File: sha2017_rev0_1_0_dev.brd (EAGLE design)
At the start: 95 x 86 mm, 193 parts, among them IC1 CP210X_USB_UART, IC2 AP7215, IC3 ESP32WROOM32, IC4 MCP73833, IC5 FXL6408, IC6 CPT112, Q1 MOSFET-PCHANNEL, Q2 MMBT2222A, Q3 MMBT2222A, Q4 MMBT2222A, Q5 MMBT2222A, Q6 SI1304 BDL, Q7 MMBT2222A, Q8 MOSFET-PCHANNEL, T1 SI2301DS, X1 JST-PH3, X2 2908-05WB-MG

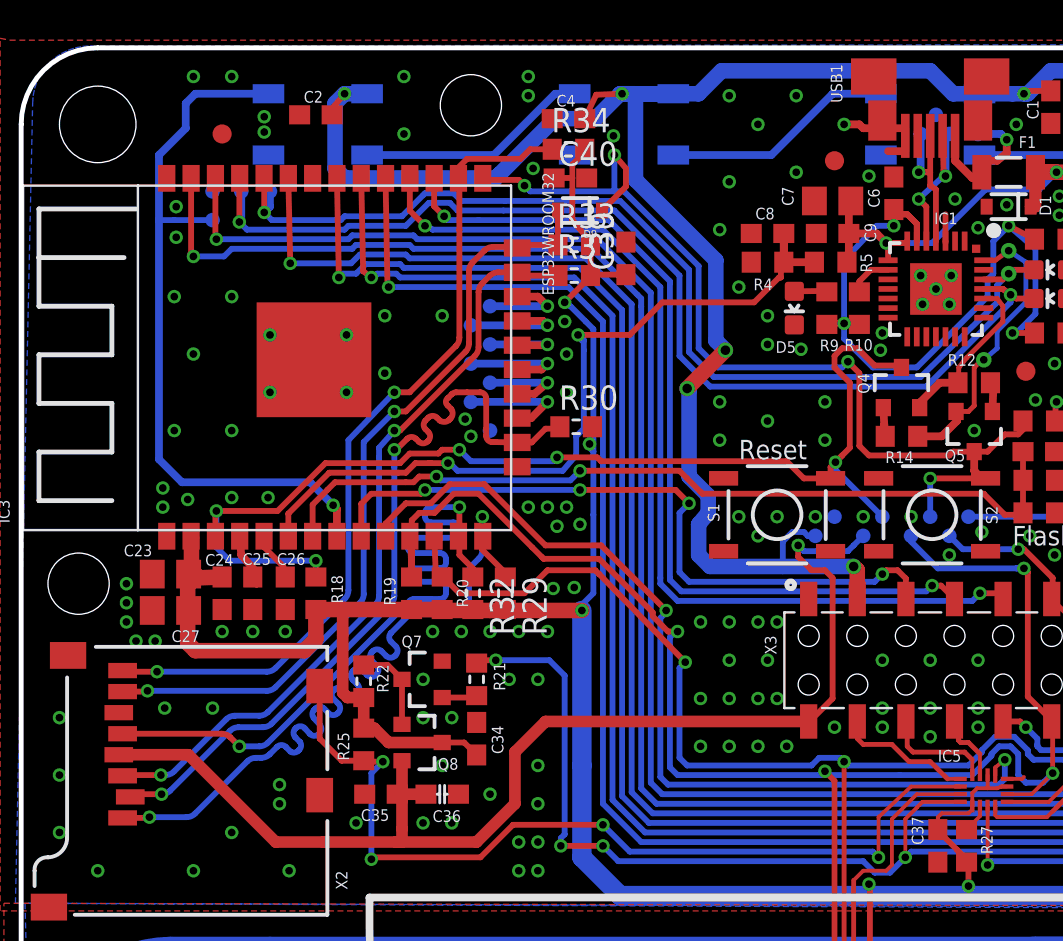
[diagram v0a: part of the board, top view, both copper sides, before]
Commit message: add solder briges to unused IOs at 1 Wire SDiomode (roosted: MIMIMI I WANT MORE IOS!!!!!)
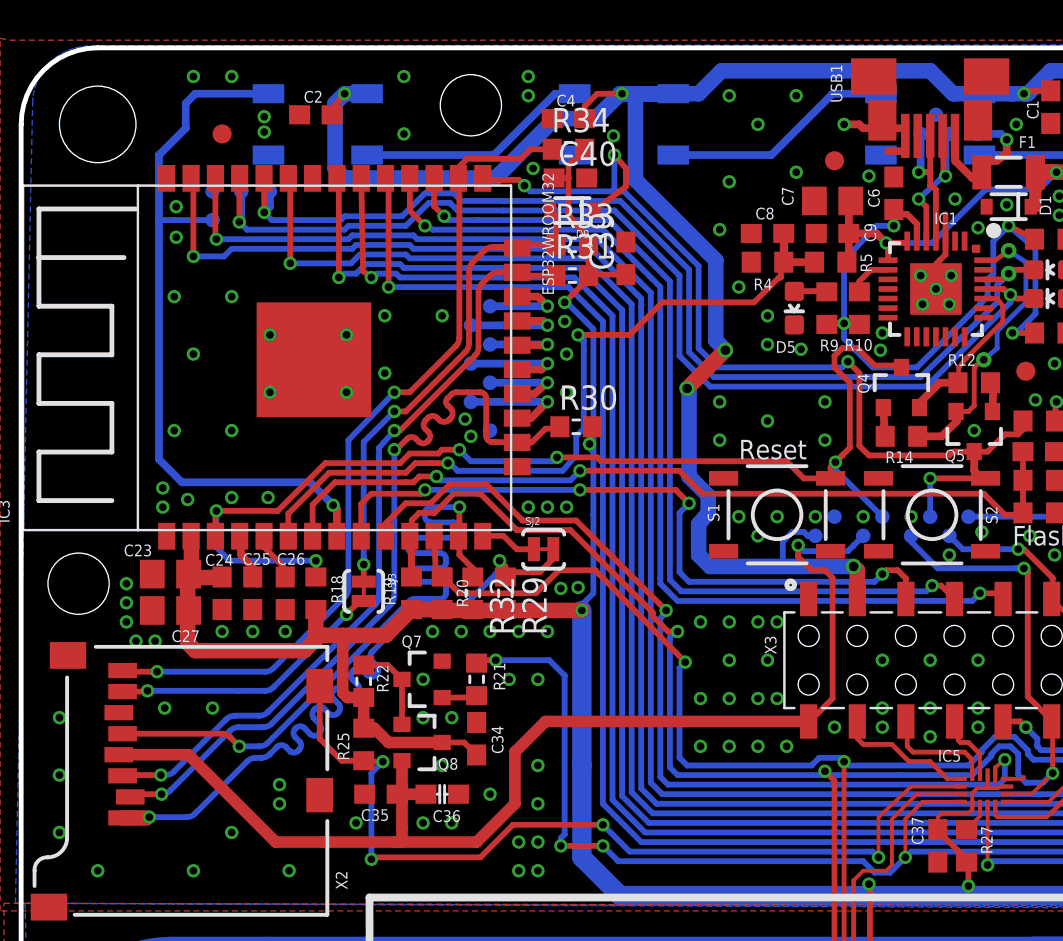
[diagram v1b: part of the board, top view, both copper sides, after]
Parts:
- added SJ2, SJ3: JUMPER-PAD-2-NC_BY_TRACE, SparkFun-Passives:PAD-JUMPER-2-NC_BY_TRACE_YES_SILK
- moved D9 0.40 mm to (28.8, 76.5)
- moved R31 0.10 mm to (28.8, 73.1)
- moved R33 0.10 mm to (28.8, 74.7)
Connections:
- new net N$20: SJ3.2, X2.7
- new net SD_DATA2_OUT: R29.1, SJ2.2, X2.1
- net SD_DATA0: now also SJ3.1; no longer X2.7
- net SD_DATA2: now also SJ2.1; no longer R29.1, X2.1
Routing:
- net SD_DATA2_OUT: track 0.00 -> 36.1 mm, vias 0 -> 2
- net SD_DATA2: track 38.5 -> 2.97 mm, vias 2 -> 0
- net SD_DATA0: track 41.4 -> 26.4 mm
- net N$20: track 0.00 -> 14.5 mm, vias 0 -> 2
- net GND: track 13.8 -> 15.0 mm, vias 276 -> 274
- net +3V3: track 270.4 -> 269.8 mm

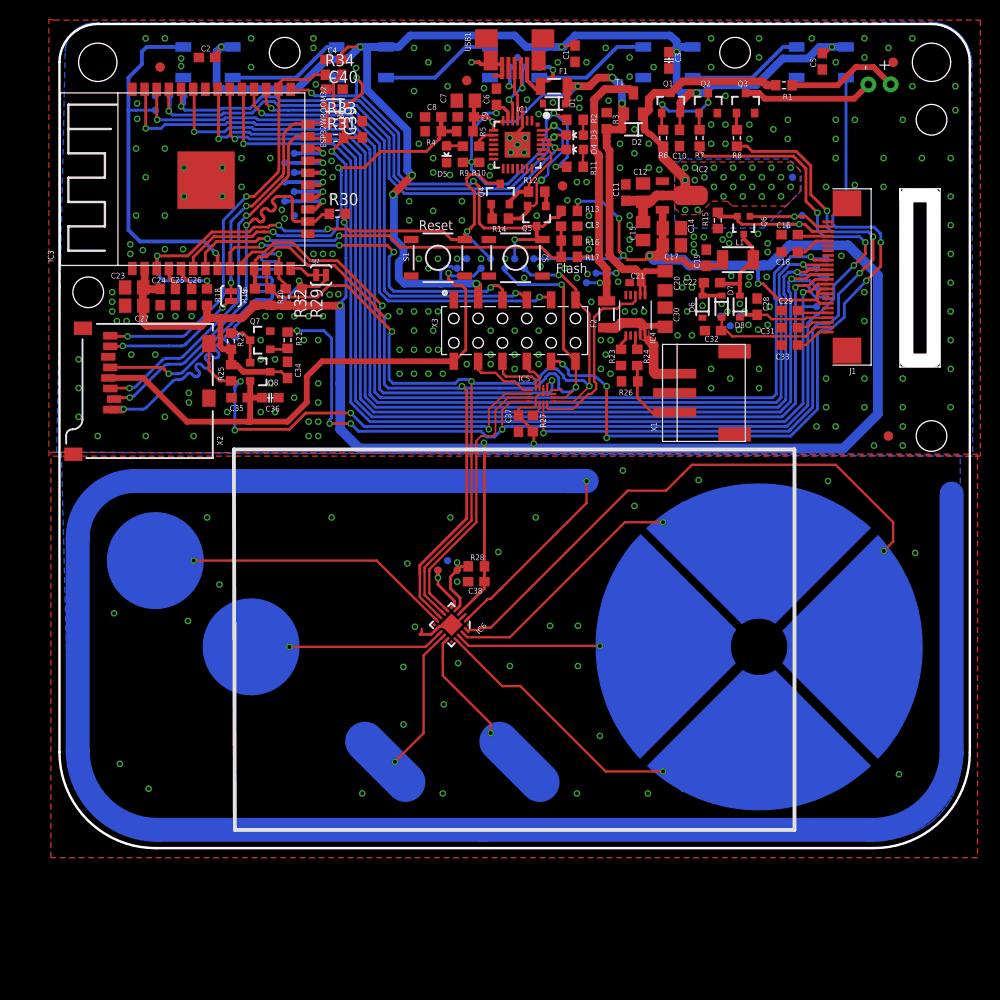
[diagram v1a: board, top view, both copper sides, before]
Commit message: fixed designators
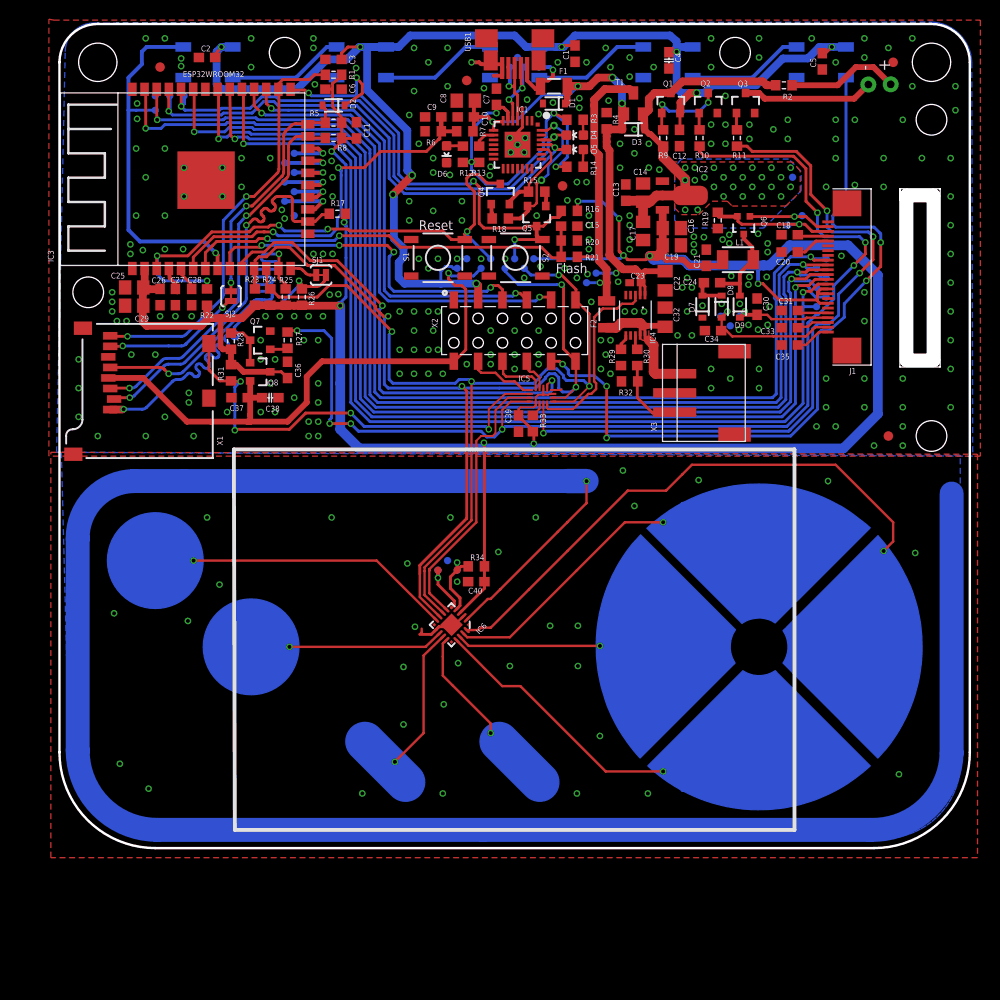
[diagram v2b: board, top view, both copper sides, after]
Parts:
- removed SJ3: JUMPER-PAD-2-NC_BY_TRACE, SparkFun-Passives:PAD-JUMPER-2-NC_BY_TRACE_YES_SILK
- removed U$26, U$27, U$28: VIA, badge:VIA
- added $$U$1, $$U$2, $$U$3: VIA, badge:VIA
- added SJ1: JUMPER-PAD-2-NC_BY_TRACE, SparkFun-Passives:PAD-JUMPER-2-NC_BY_TRACE_YES_SILK
- C12, C15, C7: value 4u7/16V -> 100n; device rcl:C0805 -> rcl:C0603
- C16, C29: value 1u -> 4u7/16V; device rcl:C0603 -> rcl:C0805
- C19, C8: value 100n -> 4u7/16V; device rcl:C0603 -> rcl:C0805
- C20, C30: value 10uF -> 1u; device rcl:C0805K -> rcl:C0603
- C21: value 100nF -> 100n; device rcl:C0402K -> rcl:C0603
- C22, C32: value 1u -> 10uF; device rcl:C0603 -> rcl:C0805K
- C23: value 4u7/16V -> 100nF; device rcl:C0805 -> rcl:C0402K
- C24, C35: value 100n -> 1u
- C25: value (none) -> 4u7/16V; device rcl:C0603 -> rcl:C0805
- C26, C37: value (none) -> 100n
- C27: value 4u7/16V -> (none); device rcl:C0805 -> rcl:C0603
- C28: value 1u -> (none)
- C3: value 4u7/16V -> 100n; device 00ralf:C0603-DASHES -> rcl:C0603
- C36: value 4u7/16V -> 1u; device 00ralf:C0603-DASHES -> rcl:C0603
- C38, C4: value 100n -> 4u7/16V; device rcl:C0603 -> 00ralf:C0603-DASHES
- C39: value 100n -> (none)
- D3: value Yellow -> NSVR0320MW2T1G; device SparkFun-LED:LED-0603 -> SparkFun-DiscreteSemi:SOD-323
- D4: value RED -> Yellow
- D5: value green -> RED
- D6: value NSVR0320MW2T1G -> green; device SparkFun-DiscreteSemi:SOD-323 -> SparkFun-LED:LED-0603
- R1: value 10R -> 10k
- R10, R27: device rcl:R0603 -> 00ralf:R0603-DASHES
- R11, R28, R9: value 1k -> 10k; device rcl:R0603 -> 00ralf:R0603-DASHES
- R12, R14, R3: value 10k -> 1k
- R15: value 5R -> 10k; device 00ralf:R0603-DASHES -> rcl:R0603
- R16, R4: value 100k -> 10k
- R17, R5: value 220k -> 10k; device rcl:R0603 -> 00ralf:R0603-DASHES
- R19: value 470R -> 5R; device rcl:R0603 -> 00ralf:R0603-DASHES
- R2: value 1k -> 10R; device rcl:R0603 -> 00ralf:R0603-DASHES
- R20: value 470R -> 100k
- R21, R7: value 10k -> 220k; device 00ralf:R0603-DASHES -> rcl:R0603
- R22, R33: device 00ralf:R0603-DASHES -> rcl:R0603
- R23: value 2.2k -> 470R
- R24: value 1k -> 470R
- R25: value 100k -> 10k; device rcl:R0603 -> 00ralf:R0603-DASHES
- R26: value 150k -> 10k; device rcl:R0603 -> 00ralf:R0603-DASHES
- R29: value 10k -> 2.2k; device 00ralf:R0603-DASHES -> rcl:R0603
- R30, R34: value 10k -> 1k; device 00ralf:R0603-DASHES -> rcl:R0603
- R31, R6: value 10k -> 100k; device 00ralf:R0603-DASHES -> rcl:R0603
- R32: value 10k -> 150k; device 00ralf:R0603-DASHES -> rcl:R0603
- X1: value JST-PH3 -> 2908-05WB-MG; device badge:JST-PH3 -> con-3m:MICRO-SD-SOCKET-PP
- X2: value 2908-05WB-MG -> (none); device con-3m:MICRO-SD-SOCKET-PP -> EAGLE-BOARD-TO-BOARD_CONNECTORS-rev16c:610X12243021
- X3: value (none) -> JST-PH3; device EAGLE-BOARD-TO-BOARD_CONNECTORS-rev16c:610X12243021 -> badge:JST-PH3
- moved $$U$8 83.8 mm to (5.70, 23.5)
- moved C29 68.4 mm to (7.80, 55.6), turned to 180 degrees
- moved C28 59.0 mm to (13.8, 56.5), turned to 90 degrees
- moved C35 57.7 mm to (76.2, 51.5), turned to 0 degrees
- moved C24 57.6 mm to (68.1, 58.0), turned to 0 degrees
- moved C40 53.5 mm to (43.5, 26.8), turned to 180 degrees
- moved R34 53.4 mm to (43.5, 28.4)
- moved C23 52.3 mm to (60.1, 58.0), turned to 0 degrees
- moved U$20 52.0 mm to (87.6, 6.70)
- moved R19 49.0 mm to (68.7, 64.5), turned to 270 degrees
- moved X1 48.7 mm to (16.0, 53.7), turned to 90 degrees
- moved U$11 48.4 mm to (54.1, 22.2)
- moved U$23 47.6 mm to (40.0, 4.70)
- moved U$21 47.4 mm to (9.30, 5.20)
- moved D9 47.1 mm to (71.0, 55.5), turned to 90 degrees
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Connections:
- net +3V3: now also C11.1, C16.1, C21.1, C25.1, C26.1, C29.1, C36.1, C6.1, R1.2, R16.2, R17.2, R22.1, R23.1, R24.1, R25.2, R26.2, R31.1, R33.1, R5.2, R8.2; no longer C14.1, C17.1, C23.1, C24.1, C27.1, C34.1, C37.1, C38.1, R13.2, R18.1, R19.1, R20.1, R22.2, R25.1, R27.1, R29.2, R30.2, R31.2, R32.2, R33.2
- net +5V: now also C10.1, C22.2, C23.2, C8.1, D3.A, R4.2, R7.2; no longer C20.2, C21.2, C7.1, C9.1, D2.A, R3.2, R5.2
- net 3V3_SWITCHED: now also C37.1, C38.1, X1.4, X2.12; no longer C35.1, C36.1, X2.4, X3.12
- net ESP32_!RESET: now also R22.2; no longer R18.2
- net ESP32_FLASH: now also D2.C, R16.1; no longer D9.C, R13.1
- net ESP32_RX: now also D4.C; no longer D3.C
- net ESP32_TX: now also D5.C; no longer D4.C
- net EXTIO-0: now also X2.3; no longer X3.3
- net EXTIO-1: now also X2.4; no longer X3.4
- net EXTIO-2: now also X2.5; no longer X3.5
- net EXTIO-3: now also X2.9; no longer X3.9
- net EXTIO-4: now also X2.10; no longer X3.10
- net EXTIO-5: now also X2.11; no longer X3.11
- net GND: now also $$U$1.P$1, $$U$2.P$1, $$U$3.P$1, C10.2, C12.1, C16.2, C21.2, C22.1, C23.1, C25.2, C26.2, C27.1, C29.2, C3.1, C34.1, C35.1, C4.2, D7.C, R19.2, R20.1, R29.1, R32.1, R6.1, X1.6, X1.CD2, X1.GND1, X1.GND3, X2.1, X3.2; no longer C10.1, C12.2, C16.1, C21.1, C23.2, C24.2, C25.1, C26.1, C27.2, C29.1, C3.2, C34.2, C35.2, C4.1, D5.C, R15.2, R16.1, R23.1, R26.1, R3.1, U$26.P$1, U$27.P$1, U$28.P$1, X1.2, X2.6, X2.CD2, X2.GND1, X2.GND3, X3.1
- net I2C_SCL: now also R24.2, X2.6; no longer R20.2, X3.6
- net I2C_SDA: now also R23.2, X2.7; no longer R19.2, X3.7
- net N$10: now also R15.1; no longer R12.1
- net N$11: now also R18.1; no longer R14.1
- net N$13: now also R15.2; no longer R12.2
- net N$14: now also R18.2; no longer R14.2
- net N$15: now also R27.2; no longer R21.2
- net N$17: now also R28.1; no longer R22.1
- net N$18: now also R2.1; no longer R1.1
- net N$20: now also SJ2.2, X1.7; no longer SJ3.2, X2.7
- net N$22: now also C24.1, D7.A, D8.C; no longer C22.1, D6.A, D7.C
- net N$23: now also C24.2, D9.A; no longer C22.2, D8.A
- net N$26: now also D6.A, R12.1; no longer D5.A, R9.1
- net N$27: now also D4.A, R3.1; no longer D3.A, R2.1
- net N$28: now also D5.A, R14.1; no longer D4.A, R11.1
- net N$42: now also C27.2; no longer C25.2
- net N$43: now also C28.2; no longer C26.2
- net N$45: now also R11.1; no longer R8.1
- net N$46: now also R29.2; no longer R23.2
- net N$47: now also R30.2; no longer R24.2
- net N$48: now also R30.1, R32.2, X3.1; no longer R24.1, R26.2, X1.1
- net N$49: now also C32.2, X3.3; no longer C30.2, X1.3
- net N$52: now also R10.2; no longer R7.2
- net N$53: now also R9.1; no longer R6.1
- net N$59: now also R33.2; no longer R27.2
- net N$61: now also R34.1; no longer R28.1
- net N$8: now also R13.2; no longer R10.2
- net PREVGH: now also C30.2, D9.C; no longer C28.2, D8.C
- net PREVGL: now also C34.2, D8.A; no longer C32.2, D7.A
- net RESE: now also R19.1; no longer R15.1
- net SD_CD: now also R31.2, X1.CD1; no longer R25.2, X2.CD1
- net SD_CLK: now also R25.1, X1.5; no longer R32.1, X2.5
- net SD_CMD: now also R8.1, X1.3; no longer R31.1, X2.3
- net SD_DATA0: now also D2.A, R5.1, SJ2.1; no longer D9.A, R33.1, SJ3.1
- net SD_DATA1: now also R1.1, X1.8; no longer R34.1, X2.8
- net SD_DATA2: now also SJ1.1; no longer SJ2.1
- net SD_DATA2_OUT: now also R26.1, SJ1.2, X1.1; no longer R29.1, SJ2.2, X2.1
- net SD_DATA3: now also R17.1, X1.2; no longer R30.1, X2.2
- net VBAT: now also R21.2; no longer R17.2
- net VBAT_SENSE: now also C15.1, R20.2, R21.1; no longer C13.1, R16.2, R17.1
- net VCC: now also C13.1, C14.1, C17.1, D3.C, R2.2, R9.2; no longer C11.1, C12.1, C15.1, D2.C, R1.2, R6.2
- net VCOM: now also C35.2; no longer C33.2
- net VDD: now also C7.1, R12.2, R13.1, R14.2, R3.2; no longer C6.1, R10.1, R11.2, R2.2, R9.2
- net VGH: now also C20.2; no longer C18.2
- net VGL: now also C18.2; no longer C16.2
- net VIBRATOR: now also R11.2; no longer R8.2
- net VSH: now also C31.2; no longer C29.2
- net VSL: now also C33.2; no longer C31.2
- net VUSB_SENSE: now also C9.1, R6.2, R7.1; no longer C8.1, R4.2, R5.1
- net WS2812_DATA_OUT: now also X2.8; no longer X3.8
- net WS2812_POWER: now also C12.2, C3.2, C4.1, X2.2; no longer C10.2, C3.1, C4.2, X3.2
- net WS2812_POWER_EN: now also R10.1, R27.1; no longer R21.1, R7.1

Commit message: some small fixes
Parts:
- moved TP132 2.12 mm to (8.50, 77.5)
- renumbered J1 to X4
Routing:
- net WS2812_DATA: track 38.3 -> 36.8 mm
- net GND: vias 274 -> 281
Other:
- outline, holes or cut-outs redrawn
- board text added: "RX"
- board text added: "TX"
- board text added: "USB"

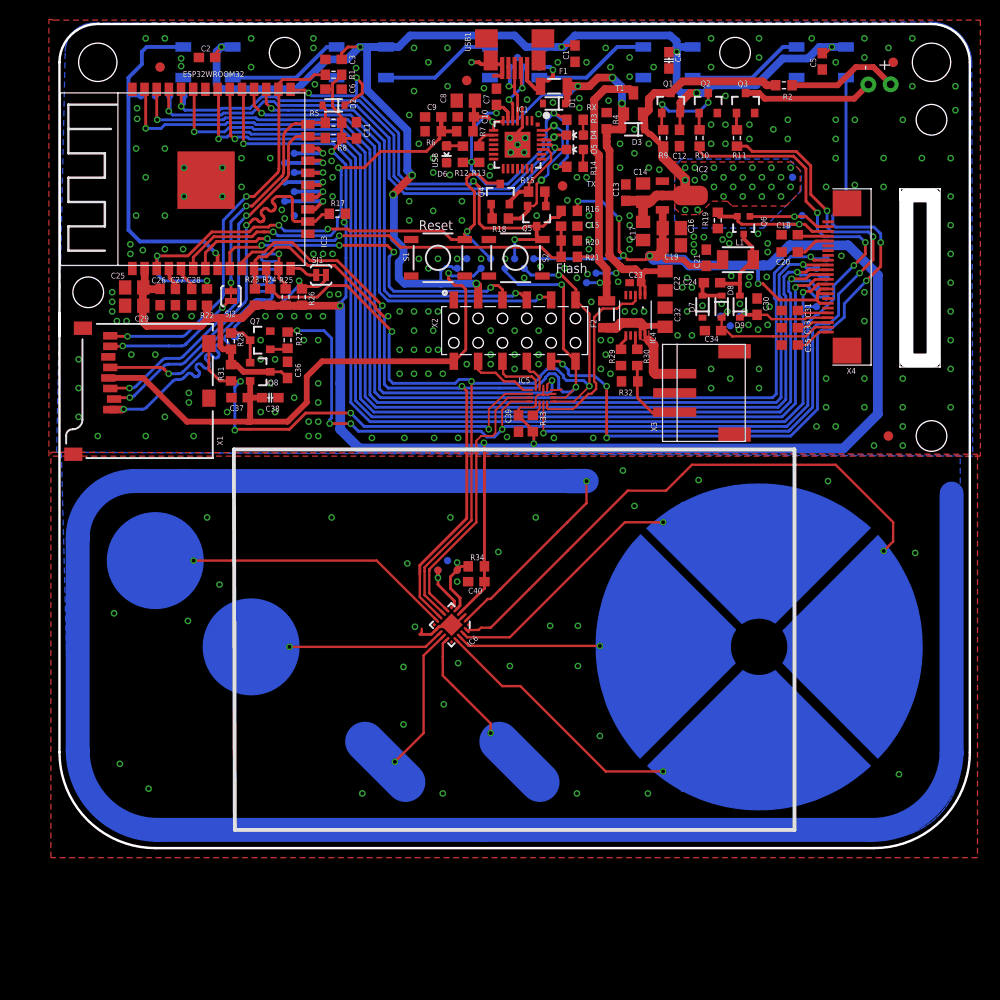
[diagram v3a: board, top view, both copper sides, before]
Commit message: cleanup an Testpoint marking
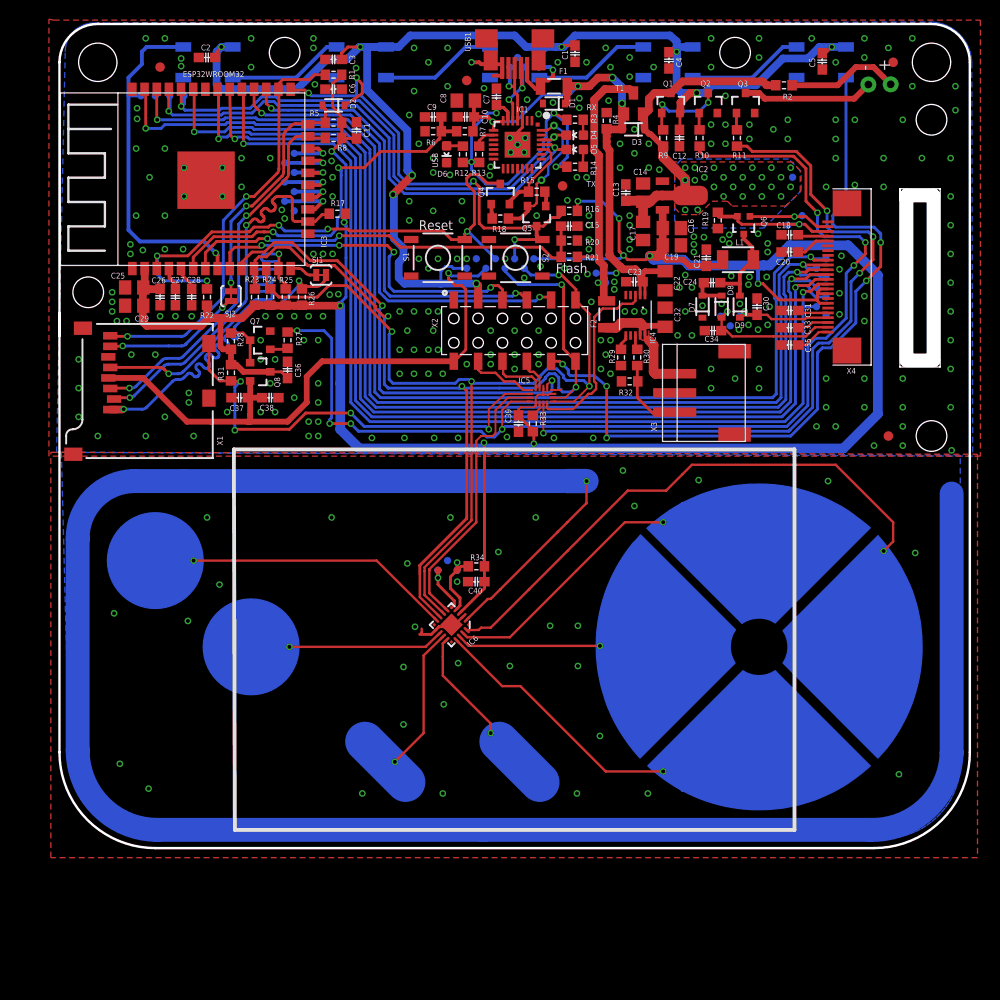
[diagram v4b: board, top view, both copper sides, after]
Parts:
- added TP5: TEST-POINT3, SparkFun-Passives:PAD.03X.03
- C1, C10, C11, C12, C13, C15, C18, C2, C20, C21, C24, C26, C3, C30, C31, C33, C34, C35, C36, C37, C39, C40, C5, C6, C7, C9: device rcl:C0603 -> sha2017_rev0_1_0_dev:C0603-DASHES
- C22, C32: value 10uF -> 10u
- C23: value 100nF -> 100n; device rcl:C0402K -> sha2017_rev0_1_0_dev:C0603-DASHES
- C27, C28: value (none) -> 100n; device rcl:C0603 -> sha2017_rev0_1_0_dev:C0603-DASHES
- R12, R13, R14, R15, R16, R18, R20, R21, R22, R23, R24, R29, R3, R30, R31, R32, R33, R34, R4, R6, R7: device rcl:R0603 -> sha2017_rev0_1_0_dev:R0603-DASHES
- R17, R19, R25, R26: device 00ralf:R0603-DASHES -> sha2017_rev0_1_0_dev:R0603-DASHES
- moved TP109 2.00 mm to (57.0, 58.0)
- moved TP116 1.00 mm to (42.5, 59.5)
- moved TP121 1.00 mm to (43.5, 60.5)
- moved TP115 0.50 mm to (44.5, 59.5)
- moved TP120 0.50 mm to (45.5, 60.5)
- moved TP124 0.50 mm to (24.5, 65.5)
- moved C23 0.14 mm to (60.0, 58.1)
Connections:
- net N$12 renamed SD1
- net N$3 renamed SD2
- net N$4 renamed SD3
- net N$6 renamed CND
- net N$7 renamed CLK
- net N$9 renamed CD0
- net GND: now also TP5.P$1
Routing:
- net WS2812_POWER: track 147.5 -> 148.5 mm
- net WS2812_POWER_EN: track 115.5 -> 116.0 mm
- net 3V3_SWITCHED: track 63.4 -> 63.9 mm
- net GND: vias 281 -> 286
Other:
- board text added: "+3V3"
- board text added: "3V3_SWITCHED"
- board text added: "5V"
- board text added: "CD0"
- board text added: "CLK"
- board text added: "CND"
- board text added: "ESP32_!RESET"
- board text added: "ESP32_FLASH"
- board text added: "ESP32_RX"
- board text added: "ESP32_TX"
- board text added: "GDR"
- board text added: "GND"
- board text added: "I2C_SCL"
- board text added: "I2C_SDA"
- board text added: "LCD_!RESET"
- board text added: "LCD_BUSY"
- board text added: "LCD_CS"
- board text added: "LCD_D/!S"
- board text added: "LCD_MOSI"
- board text added: "LCD_SCK"
- board text added: "PREVGH"
- board text added: "PREVGL"
- board text added: "RESE"
- board text added: "SD1"
- board text added: "SD2"
- board text added: "SD3"
- board text added: "USB_DN_CON"
- board text added: "USB_DP_CON"
- board text added: "VBAT"
- board text added: "VCC"
- board text added: "VUSB_IN"
- board text added: "WS2812_DATA"
- board text added: "WS2812_POWER"
